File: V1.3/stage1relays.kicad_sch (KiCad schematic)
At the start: 14 parts, among them T3 AO3400A, T4 AO3400A

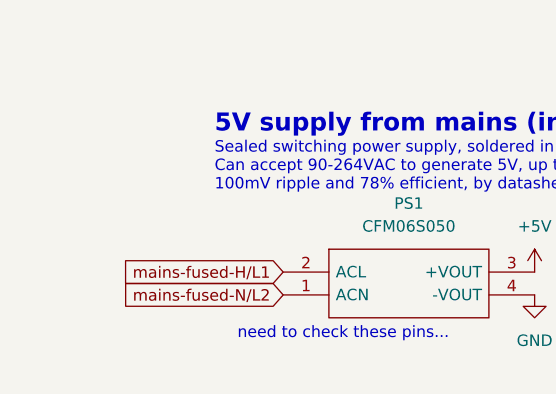
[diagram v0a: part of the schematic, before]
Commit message: clarify door-activator role || Active & Passive door operation
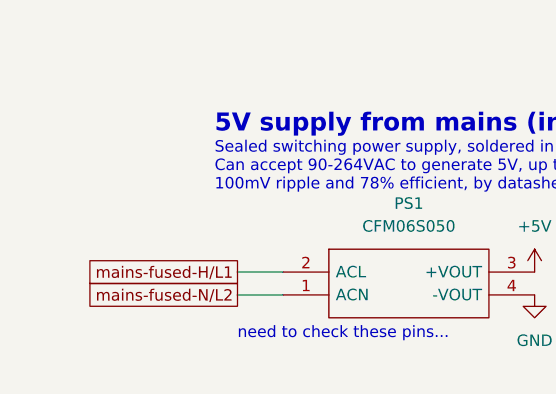
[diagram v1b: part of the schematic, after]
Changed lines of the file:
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@@
+    (stroke (width 0) (type default) (color 0 0 0 0))
+  )
+  (wire (pts (xy 54.61 163.83) (xy 49.53 163.83))
     (stroke (width 0) (type default) (color 0 0 0 0))
   )
@@
   )
   (wire (pts (xy 193.04 95.25) (xy 193.04 91.44))
+    (stroke (width 0) (type default) (color 0 0 0 0))
+  )
+  (wire (pts (xy 54.61 166.37) (xy 49.53 166.37))
     (stroke (width 0) (type default) (color 0 0 0 0))
   )
@@
     )
   )
-  (global_label "mains-fused-N{slash}L2" (shape input) (at 54.61 166.37 180) (fields_autoplaced)
-    (effects (font (size 1.27 1.27)) (justify right))
-    (property "Intersheet References" "${INTERSHEET_REFS}" (id 0) (at 33.3888 166.2906 0)
-      (effects (font (size 1.27 1.27)) (justify right) hide)
-    )
-  )
   (global_label "set3v" (shape input) (at 55.88 102.87 180) (fields_autoplaced)
     (effects (font (size 1.27 1.27)) (justify right))
@@
     )
   )
-  (global_label "mains-fused-H{slash}L1" (shape input) (at 54.61 163.83 180) (fields_autoplaced)
-    (effects (font (size 1.27 1.27)) (justify right))
-    (property "Intersheet References" "${INTERSHEET_REFS}" (id 0) (at 33.3888 163.7506 0)
-      (effects (font (size 1.27 1.27)) (justify right) hide)
-    )
-  )
   (global_label "read-bypass" (shape output) (at 93.98 97.79 0) (fields_autoplaced)
     (effects (font (size 1.27 1.27)) (justify left))
@@
     )
   )
+  (global_label "mains-fused-N{slash}L2" (shape passive) (at 49.53 166.37 180) (fields_autoplaced)
+    (effects (font (size 1.27 1.27)) (justify right))
+    (property "Intersheet References" "${INTERSHEET_REFS}" (id 0) (at 28.3088 166.4494 0)
+      (effects (font (size 1.27 1.27)) (justify right) hide)
+    )
+  )
+  (global_label "mains-fused-H{slash}L1" (shape passive) (at 49.53 163.83 180) (fields_autoplaced)
+    (effects (font (size 1.27 1.27)) (justify right))
+    (property "Intersheet References" "${INTERSHEET_REFS}" (id 0) (at 28.3088 163.9094 0)
+      (effects (font (size 1.27 1.27)) (justify right) hide)
+    )
+  )
